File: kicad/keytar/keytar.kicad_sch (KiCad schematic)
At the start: 36 parts, among them J1 , J2 USB_B, J3 AudioJack2, J4 Conn_01x04, J5 USB_A, J6 Mini-DIN-6-Shielded, J7 Conn_01x04, Q1 BSS138, Q2 BSS138, SW1 SW_DPST_x2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

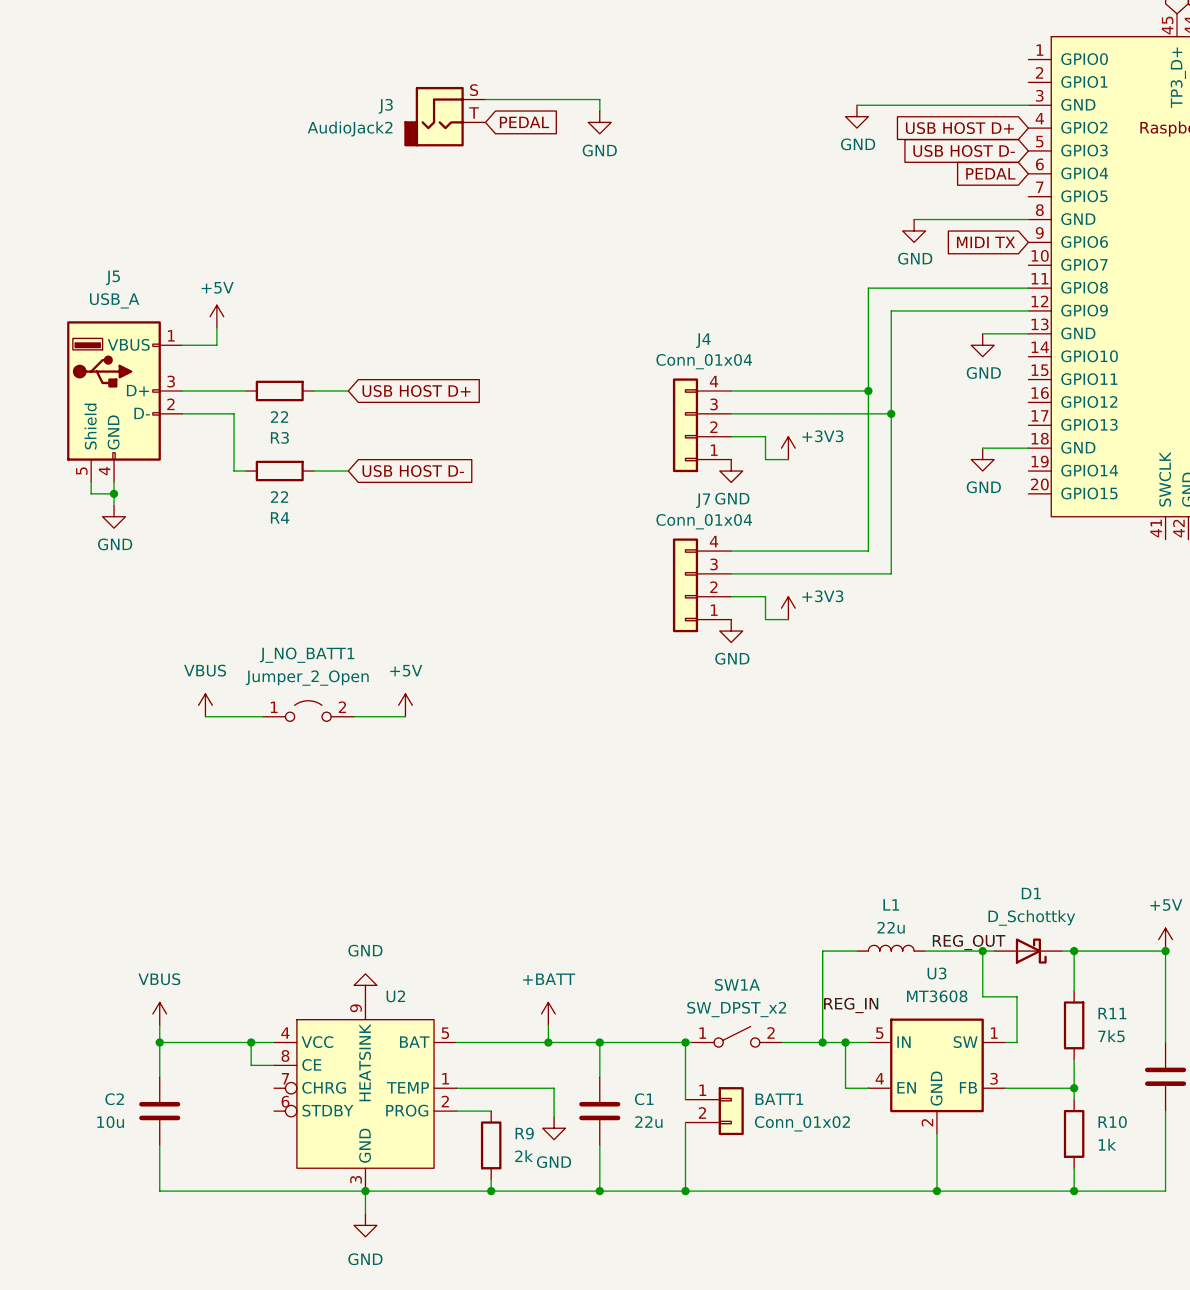
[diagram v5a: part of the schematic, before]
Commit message: add traces to read charger status
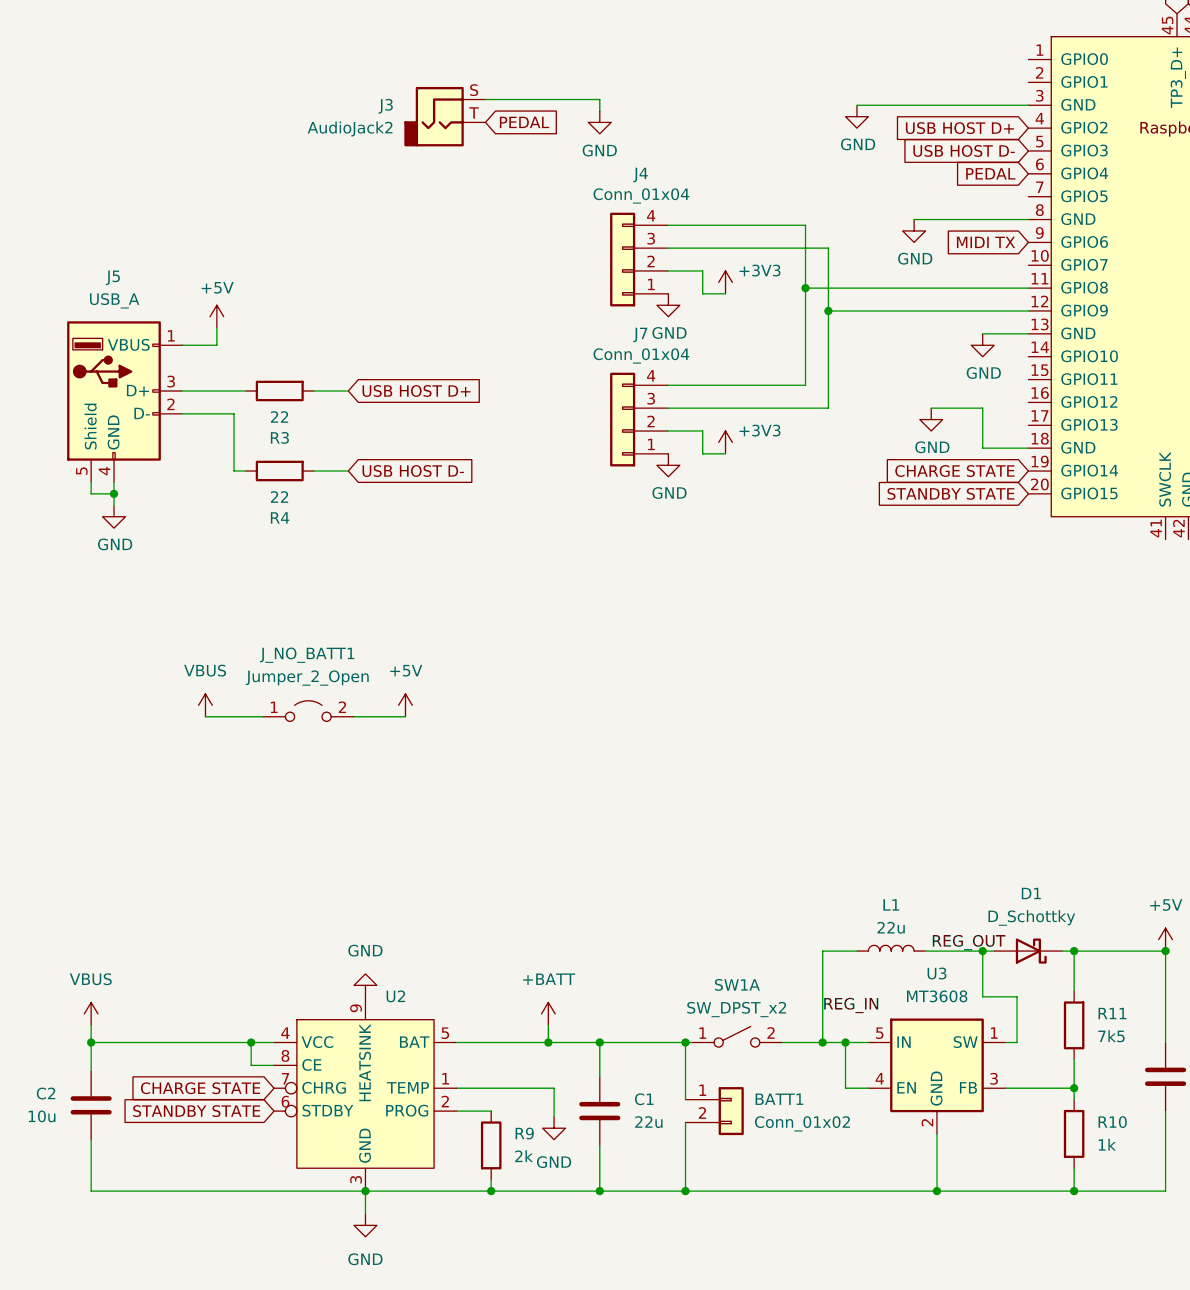
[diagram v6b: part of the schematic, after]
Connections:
- net CHARGE STATE: now reaches U1.19 (GPIO14)
- net CHARGE STATE: now also U2.7 (CHRG)
- net STANDBY STATE: now reaches U1.20 (GPIO15)
- net STANDBY STATE: now also U2.6 (STDBY)
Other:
- moved on the sheet: C2, J4, J7

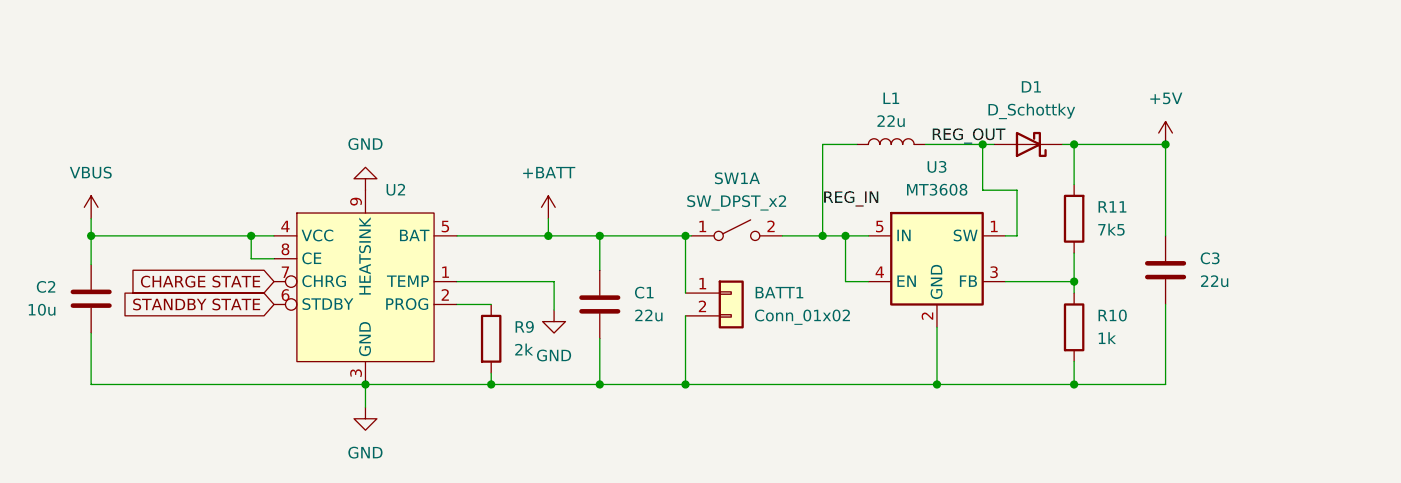
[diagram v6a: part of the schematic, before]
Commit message: kicad: use proper capacitors
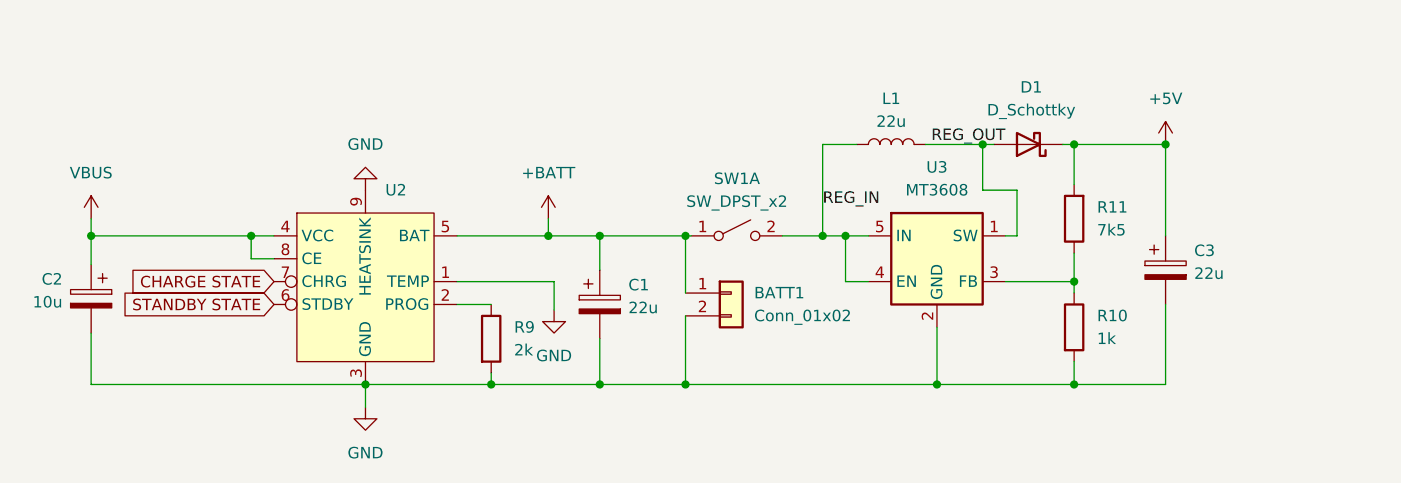
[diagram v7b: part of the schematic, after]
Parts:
- removed C1, C3: 22u, Capacitor_SMD:C_1206_3216Metric_Pad1.33x1.80mm_HandSolder, symbol Device:C
- removed C2: 10u, Capacitor_SMD:C_1206_3216Metric_Pad1.33x1.80mm_HandSolder, symbol Device:C
- added C1, C3: 22u, Capacitor_SMD:CP_Elec_4x5.3, symbol Device:C_Polarized
- added C2: 10u, Capacitor_SMD:CP_Elec_4x5.3, symbol Device:C_Polarized
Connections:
- net +5V: now also C3.1
- net +BATT: now also C1.1
- net GND: now also C1.2, C2.2, C3.2
- net VBUS: now also C2.1
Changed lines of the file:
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@@
+    )
+  )
+  (symbol (lib_id "Device:C_Polarized") (at 79.375 172.72 0) (unit 1)
+    (in_bom yes) (on_board yes) (dnp no) (fields_autoplaced)
+    (property "Reference" "C1" (at 82.55 170.561 0)
+      (effects (font (size 1.27 1.27)) (justify left))
+    )
+    (property "Value" "22u" (at 82.55 173.101 0)
+      (effects (font (size 1.27 1.27)) (justify left))
+    )
+    (property "Footprint" "Capacitor_SMD:CP_Elec_4x5.3" (at 80.3402 176.53 0)
+      (effects (font (size 1.27 1.27)) hide)
+    )
+    (property "Datasheet" "~" (at 79.375 172.72 0)
+      (effects (font (size 1.27 1.27)) hide)
+    )
+    (pin "1")
+    (pin "2")
+    (instances
+      (project "keytar"
+        (path "/fe683dc2-37f6-494a-a02f-1dab10080979"
+          (reference "C1") (unit 1)
+        )
+      )
     )
   )
@@
     )
   )
-  (symbol (lib_id "Device:C") (at 142.24 168.91 0) (unit 1)
-    (in_bom yes) (on_board yes) (dnp no) (fields_autoplaced)
-    (property "Reference" "C3" (at 146.05 167.64 0)
-      (effects (font (size 1.27 1.27)) (justify left))
-    )
-    (property "Value" "22u" (at 146.05 170.18 0)
-      (effects (font (size 1.27 1.27)) (justify left))
-    )
-    (property "Footprint" "Capacitor_SMD:C_1206_3216Metric_Pad1.33x1.80mm_HandSolder" (at 143.2052 172.72 0)
+  (symbol (lib_id "Device:D_Schottky") (at 38.1 31.115 90) (mirror x) (unit 1)
+    (in_bom yes) (on_board yes) (dnp no)
+    (property "Reference" "D2" (at 35.56 29.5275 90)
+      (effects (font (size 1.27 1.27)) (justify left))
+    )
+    (property "Value" "D_Schottky" (at 35.56 32.0675 90)
+      (effects (font (size 1.27 1.27)) (justify left))
+    )
+    (property "Footprint" "Diode_SMD:D_SMA" (at 38.1 31.115 0)
+      (effects (font (size 1.27 1.27)) hide)
+    )
+    (property "Datasheet" "~" (at 38.1 31.115 0)
+      (effects (font (size 1.27 1.27)) hide)
+    )
+    (pin "1")
+    (pin "2")
+    (instances
+      (project "keytar"
+        (path "/fe683dc2-37f6-494a-a02f-1dab10080979"
+          (reference "D2") (unit 1)
+        )
+      )
+    )
+  )
+  (symbol (lib_id "Device:C_Polarized") (at 142.24 168.91 0) (unit 1)
+    (in_bom yes) (on_board yes) (dnp no) (fields_autoplaced)
+    (property "Reference" "C3" (at 145.415 166.751 0)
+      (effects (font (size 1.27 1.27)) (justify left))
+    )
+    (property "Value" "22u" (at 145.415 169.291 0)
+      (effects (font (size 1.27 1.27)) (justify left))
+    )
+    (property "Footprint" "Capacitor_SMD:CP_Elec_4x5.3" (at 143.2052 172.72 0)
       (effects (font (size 1.27 1.27)) hide)
     )
@@
     )
   )
-  (symbol (lib_id "Device:D_Schottky") (at 38.1 31.115 90) (mirror x) (unit 1)
-    (in_bom yes) (on_board yes) (dnp no)
-    (property "Reference" "D2" (at 35.56 29.5275 90)
-      (effects (font (size 1.27 1.27)) (justify left))
-    )
-    (property "Value" "D_Schottky" (at 35.56 32.0675 90)
-      (effects (font (size 1.27 1.27)) (justify left))
-    )
-    (property "Footprint" "Diode_SMD:D_SMA" (at 38.1 31.115 0)
-      (effects (font (size 1.27 1.27)) hide)
-    )
-    (property "Datasheet" "~" (at 38.1 31.115 0)
-      (effects (font (size 1.27 1.27)) hide)
-    )
-    (pin "1")
-    (pin "2")
-    (instances
-      (project "keytar"
-        (path "/fe683dc2-37f6-494a-a02f-1dab10080979"
-          (reference "D2") (unit 1)
-        )
-      )
-    )
-  )
   (symbol (lib_id "power:GND") (at 25.4 105.41 0) (unit 1)
     (in_bom yes) (on_board yes) (dnp no)
@@
         (path "/fe683dc2-37f6-494a-a02f-1dab10080979"
           (reference "#PWR010") (unit 1)
-        )
-      )
-    )
-  )
-  (symbol (lib_id "Device:C") (at 79.375 172.72 0) (unit 1)
-    (in_bom yes) (on_board yes) (dnp no) (fields_autoplaced)
-    (property "Reference" "C1" (at 83.185 171.45 0)
-      (effects (font (size 1.27 1.27)) (justify left))
-    )
-    (property "Value" "22u" (at 83.185 173.99 0)
-      (effects (font (size 1.27 1.27)) (justify left))
-    )
-    (property "Footprint" "Capacitor_SMD:C_1206_3216Metric_Pad1.33x1.80mm_HandSolder" (at 80.3402 176.53 0)
-      (effects (font (size 1.27 1.27)) hide)
-    )
-    (property "Datasheet" "~" (at 79.375 172.72 0)
-      (effects (font (size 1.27 1.27)) hide)
-    )
-    (pin "1")
-    (pin "2")
-    (instances
-      (project "keytar"
-        (path "/fe683dc2-37f6-494a-a02f-1dab10080979"
-          (reference "C1") (unit 1)
         )
       )
@@
     )
   )
-  (symbol (lib_id "Device:C") (at 22.86 172.085 0) (mirror y) (unit 1)
-    (in_bom yes) (on_board yes) (dnp no)
-    (property "Reference" "C2" (at 19.05 170.815 0)
-      (effects (font (size 1.27 1.27)) (justify left))
-    )
-    (property "Value" "10u" (at 19.05 173.355 0)
-      (effects (font (size 1.27 1.27)) (justify left))
-    )
-    (property "Footprint" "Capacitor_SMD:C_1206_3216Metric_Pad1.33x1.80mm_HandSolder" (at 21.8948 175.895 0)
-      (effects (font (size 1.27 1.27)) hide)
-    )
-    (property "Datasheet" "~" (at 22.86 172.085 0)
-      (effects (font (size 1.27 1.27)) hide)
-    )
-    (pin "1")
-    (pin "2")
-    (instances
-      (project "keytar"
-        (path "/fe683dc2-37f6-494a-a02f-1dab10080979"
-          (reference "C2") (unit 1)
-        )
-      )
-    )
-  )
   (symbol (lib_id "Transistor_FET:BSS138") (at 246.38 148.59 270) (unit 1)
     (in_bom yes) (on_board yes) (dnp no) (fields_autoplaced)
@@
         )
       )
+    )
+  )
+  (symbol (lib_id "Device:C_Polarized") (at 22.86 172.085 0) (mirror y) (unit 1)
+    (in_bom yes) (on_board yes) (dnp no)
+    (property "Reference" "C2" (at 19.685 169.926 0)
+      (effects (font (size 1.27 1.27)) (justify left))
+    )
+    (property "Value" "10u" (at 19.685 172.466 0)
+      (effects (font (size 1.27 1.27)) (justify left))
+    )
+    (property "Footprint" "Capacitor_SMD:CP_Elec_4x5.3" (at 21.8948 175.895 0)
+      (effects (font (size 1.27 1.27)) hide)
+    )
+    (property "Datasheet" "~" (at 22.86 172.085 0)
+      (effects (font (size 1.27 1.27)) hide)
+    )
+    (pin "1")
+    (pin "2")
+    (instances
+      (project "keytar"
+        (path "/fe683dc2-37f6-494a-a02f-1dab10080979"
+          (reference "C2") (unit 1)
+        )
+      )

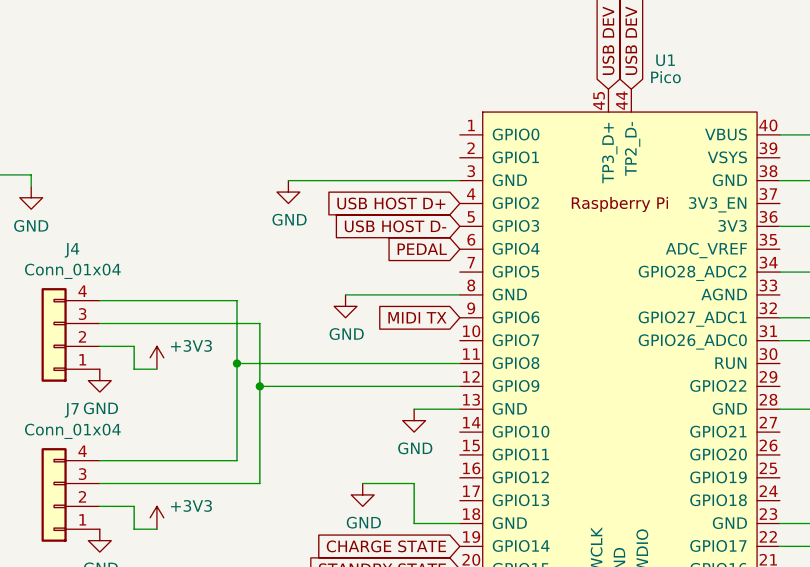
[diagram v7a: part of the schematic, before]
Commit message: pcb: adjust midi and pedal pins
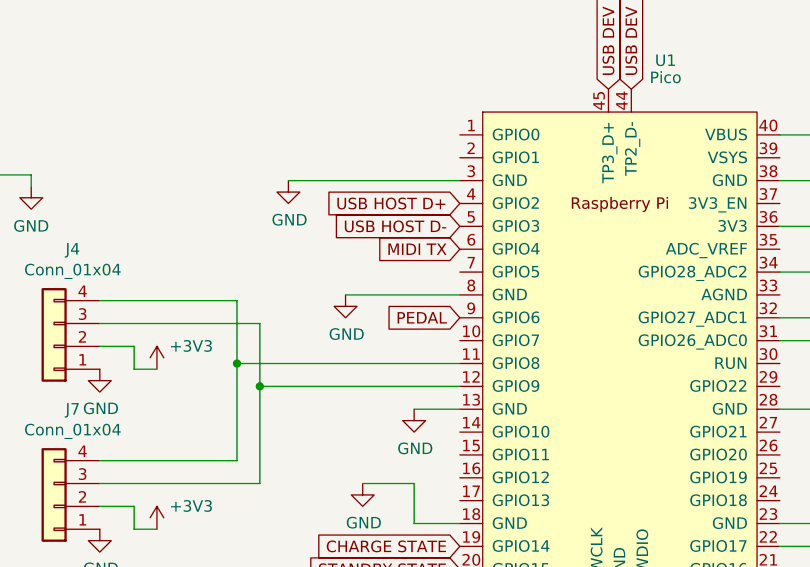
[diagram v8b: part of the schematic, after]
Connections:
- net MIDI TX: now also U1.6 (GPIO4); no longer U1.9 (GPIO6)
- net PEDAL: now also U1.9 (GPIO6); no longer U1.6 (GPIO4)
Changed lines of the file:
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@@
-    )
-  )
-  (global_label "MIDI TX" (shape input) (at 127 76.2 180) (fields_autoplaced)
-    (effects (font (size 1.27 1.27)) (justify right))
-    (property "Intersheetrefs" "${INTERSHEET_REFS}" (at 117.5933 76.2 0)
-      (effects (font (size 1.27 1.27)) (justify right) hide)
     )
   )
@@
     )
   )
+  (global_label "MIDI TX" (shape input) (at 127 68.58 180) (fields_autoplaced)
+    (effects (font (size 1.27 1.27)) (justify right))
+    (property "Intersheetrefs" "${INTERSHEET_REFS}" (at 117.5933 68.58 0)
+      (effects (font (size 1.27 1.27)) (justify right) hide)
+    )
+  )
   (global_label "CHARGE STATE" (shape input) (at 43.18 170.18 180) (fields_autoplaced)
     (effects (font (size 1.27 1.27)) (justify right))
@@
     )
   )
-  (global_label "PEDAL" (shape input) (at 127 68.58 180) (fields_autoplaced)
+  (global_label "PEDAL" (shape input) (at 127 76.2 180) (fields_autoplaced)
     (effects (font (size 1.27 1.27)) (justify right))
-    (property "Intersheetrefs" "${INTERSHEET_REFS}" (at 118.8633 68.58 0)
+    (property "Intersheetrefs" "${INTERSHEET_REFS}" (at 118.8633 76.2 0)
       (effects (font (size 1.27 1.27)) (justify right) hide)
     )
